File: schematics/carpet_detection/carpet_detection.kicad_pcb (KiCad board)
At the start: 2 copper layers, 7 parts, among them J1 Conn_01x03, U1 QRD1114, U2 TLC277

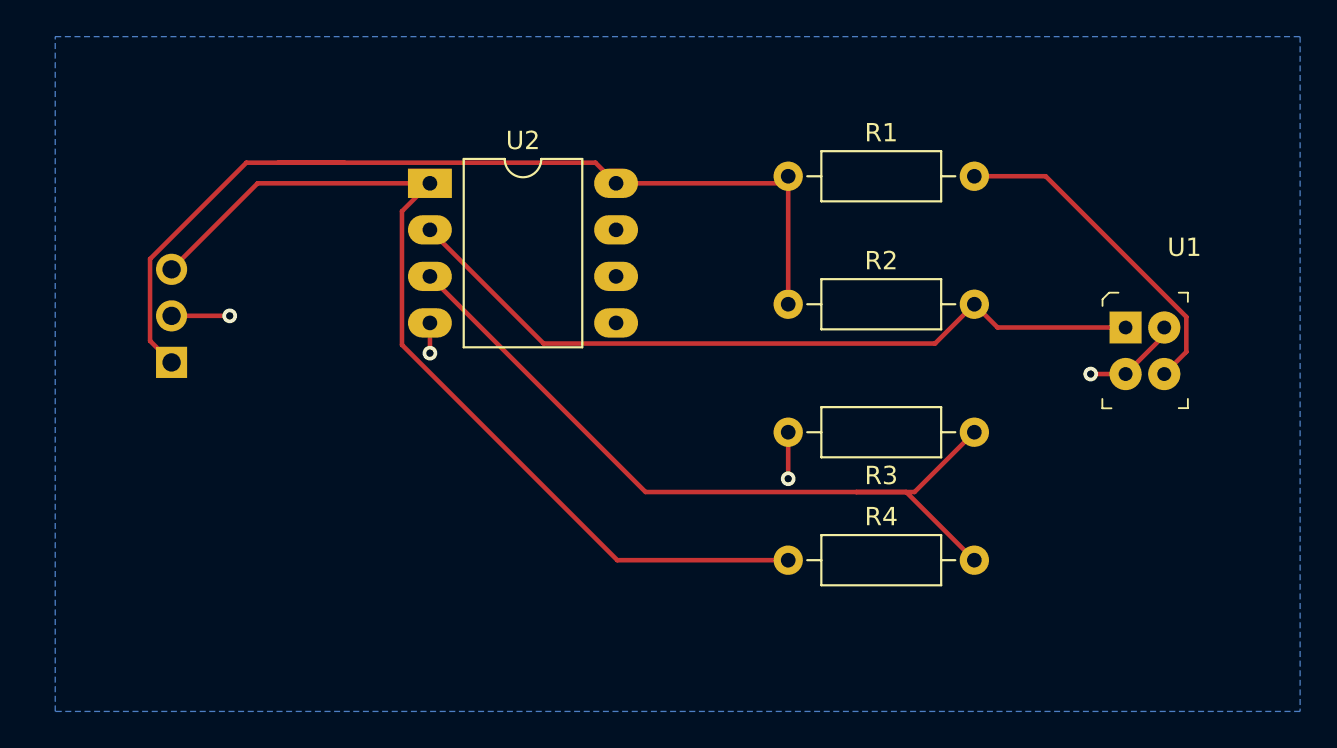
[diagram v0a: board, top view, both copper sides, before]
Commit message: Adds LEDS to the carpet detector
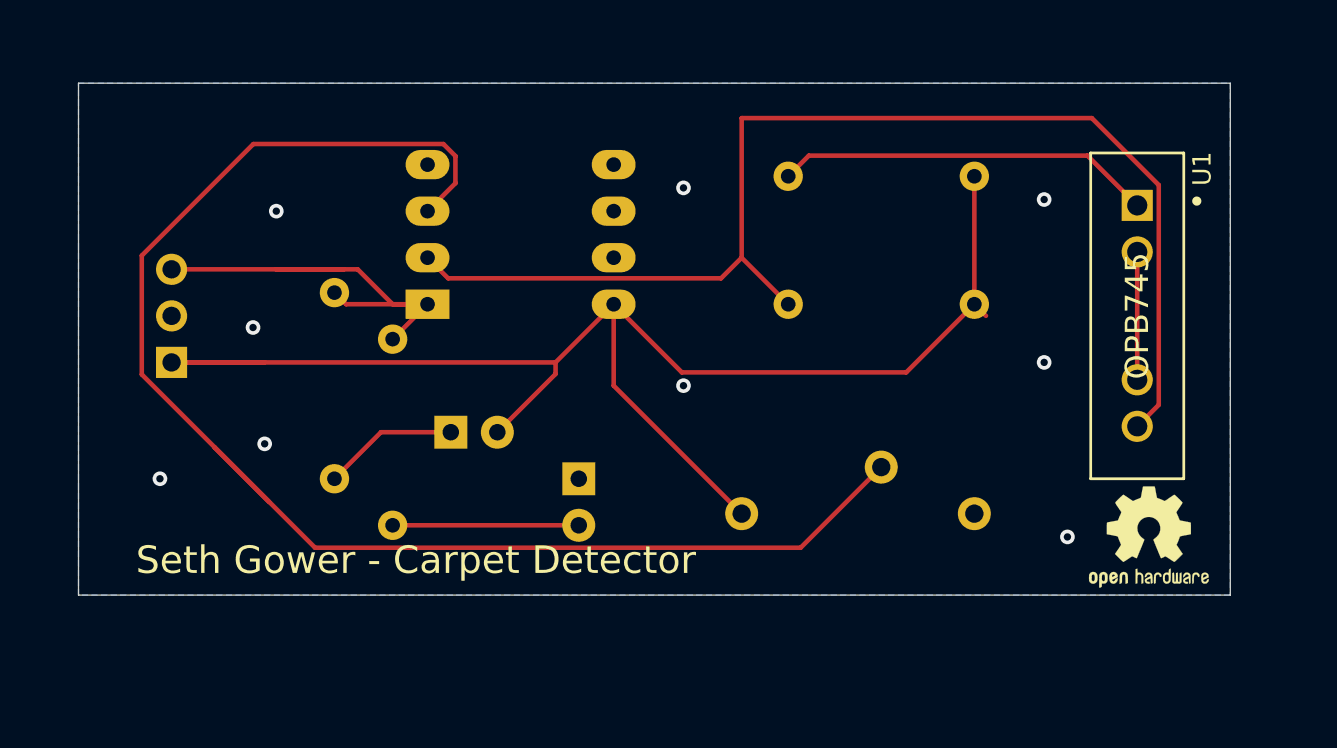
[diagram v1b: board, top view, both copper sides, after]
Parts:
- added D1: Red, LED_THT:LED_D4.0mm, B.Cu at (93.3, 101.6)
- added D2: Green, LED_THT:LED_D4.0mm, B.Cu at (100.3, 104.1)
- added REF**: OSHW-Logo2_7.3x6mm_SilkScreen, Symbol:OSHW-Logo2_7.3x6mm_SilkScreen, F.Cu at (131.4, 107.3)
- added REF**: OSHW-Logo2_7.3x6mm_SilkScreen, Symbol:OSHW-Logo2_7.3x6mm_SilkScreen, B.Cu at (131.4, 107.3)
- added RV1: R_POT_US, Potentiometer_THT:Potentiometer_Bourns_3005_Horizontal, B.Cu at (109.2, 106.0)
- R1, R2, U2: moved to B.Cu
- R3, R4: value R_US -> 1k; moved to B.Cu
- U1: value QRD1114 -> OPB745; footprint digikey-footprints:Reflective_Sensor_QRD1114 -> OPB745:TT_Electronics-OPB745-0
- moved R3 35.0 mm to (87.0, 104.1), turned to 90 degrees
- moved R4 24.7 mm to (90.2, 96.5), turned to 270 degrees
- moved R1 10.2 mm to (121.9, 87.6), turned to 180 degrees
- moved R2 10.2 mm to (121.9, 94.6), turned to 180 degrees
- moved U2 6.60 mm to (92.1, 94.6)
- moved U1 0.90 mm to (130.8, 95.2), turned to 270 degrees
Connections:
- net +5V renamed +3V3
- R2 pad 2: Net-(R2-Pad2) -> /Vin
- R3 pad 1: Net-(R3-Pad1) -> Net-(D1-Pad1)
- R3 pad 2: GND -> Vout
- R4 pad 2: Net-(R3-Pad1) -> Net-(D2-Pad2)
- U1 pad 1: Net-(R2-Pad2) -> Net-(R1-Pad2)
- U1 pad 3: Net-(R1-Pad2) -> GND
- U1 pad 4: GND -> /Vin
- U2 pad 2: Net-(R2-Pad2) -> /Vin
- U2 pad 3: Net-(R3-Pad1) -> /Vref
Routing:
- net /Vref: track 0.00 -> 80.4 mm
- net /Vin: track 0.00 -> 67.2 mm
- net Net-(R3-Pad1): track 43.9 -> 0.00 mm
- net Net-(R2-Pad2): track 42.0 -> 0.00 mm
- net +3V3: track 54.3 -> 80.5 mm
- net Vout: track 51.4 -> 26.5 mm
- net Net-(D2-Pad2): track 0.00 -> 10.2 mm
- net Net-(D1-Pad1): track 0.00 -> 7.40 mm
- net GND: track 12.7 -> 6.98 mm, vias 4 -> 9
- net Net-(R1-Pad2): track 18.4 -> 20.6 mm
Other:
- board outline added: 62.9 x 27.9 mm
- board text added: "Seth Gower - Carpet Detector"

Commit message: Removes Green LED, moves OPB745 to bottom, everything else to top
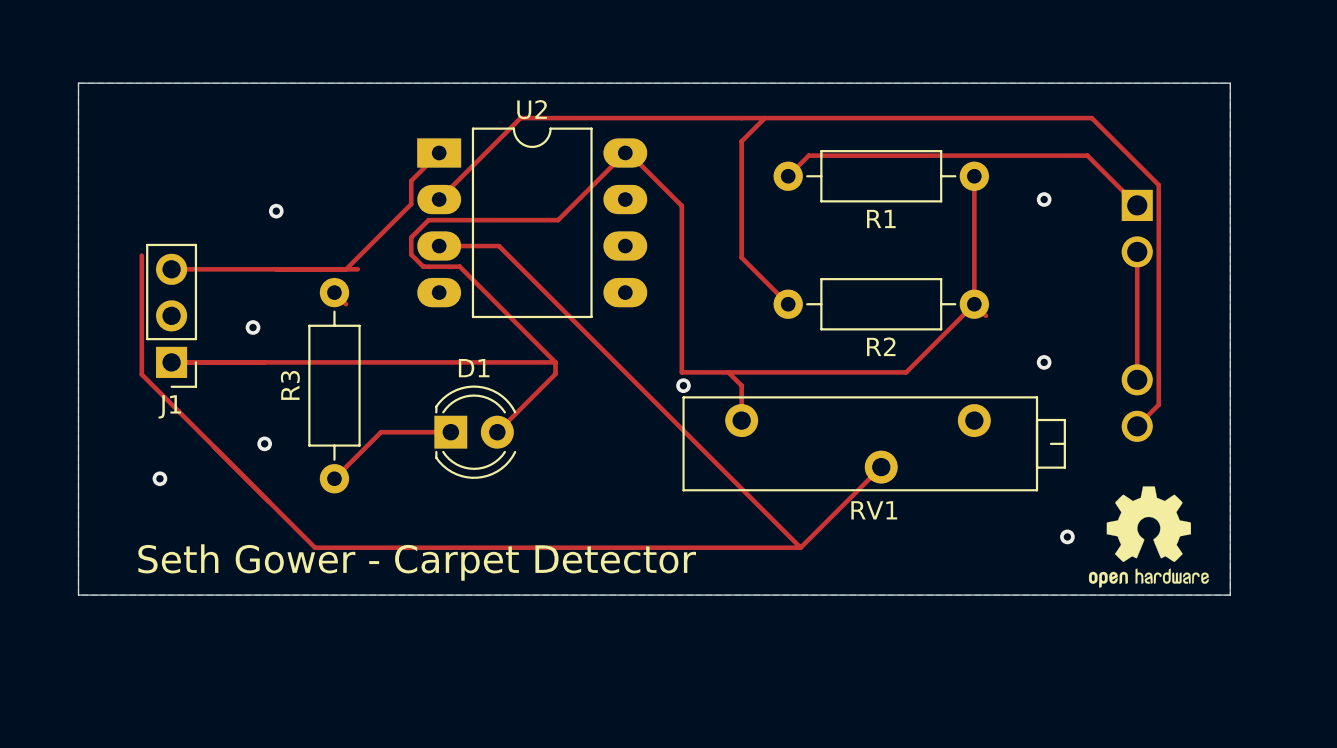
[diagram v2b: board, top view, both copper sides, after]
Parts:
- removed D2: Green, LED_THT:LED_D4.0mm
- removed R4: 1k, Resistor_THT:R_Axial_DIN0207_L6.3mm_D2.5mm_P10.16mm_Horizontal
- D1, J1, R1, R2, R3, U2: moved to F.Cu
- RV1: footprint Potentiometer_THT:Potentiometer_Bourns_3005_Horizontal -> Potentiometer_THT:Potentiometer_Bourns_3006P_Horizontal; moved to F.Cu
- U1: moved to B.Cu
- moved U2 8.28 mm to (92.7, 86.4)
- moved RV1 5.08 mm to (109.2, 101.0)
- turned J1 to 180 degrees
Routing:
- net +3V3: track 80.5 -> 97.6 mm
- net Net-(D2-Pad2): track 10.2 -> 0.00 mm
- net /Vref: track 80.4 -> 83.4 mm
- net Vout: track 26.5 -> 24.1 mm
- net /Vin: track 67.2 -> 68.0 mm
- net GND: vias 9 -> 8

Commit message: Final revision of the PCB. Ordered on OSH Park
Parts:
- D1: footprint LED_THT:LED_D4.0mm -> LED_THT:LED_D5.0mm
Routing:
- net /Vref: track 83.4 -> 29.1 mm
- net Vout: track 24.1 -> 28.2 mm
- net +3V3: track 97.6 -> 96.7 mm
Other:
- board text added: "3v3"
- board text added: "CMPE-460"
- board text added: "GND"
- board text added: "Seth Gower - Carpet Detector - 11/3/20"
- board text added: "Vout"
- board text removed: "Seth Gower - Carpet Detector"

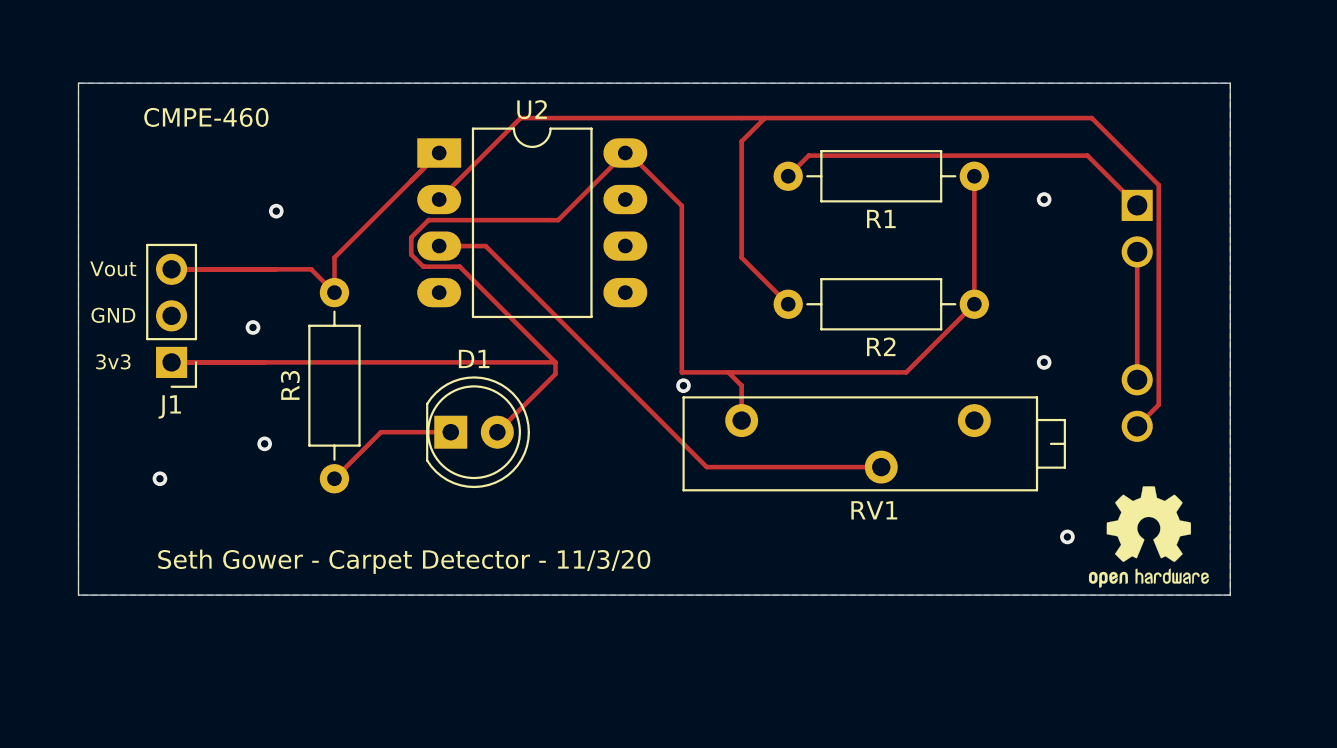
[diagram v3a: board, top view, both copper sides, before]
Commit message: Actually finishes the PCB.
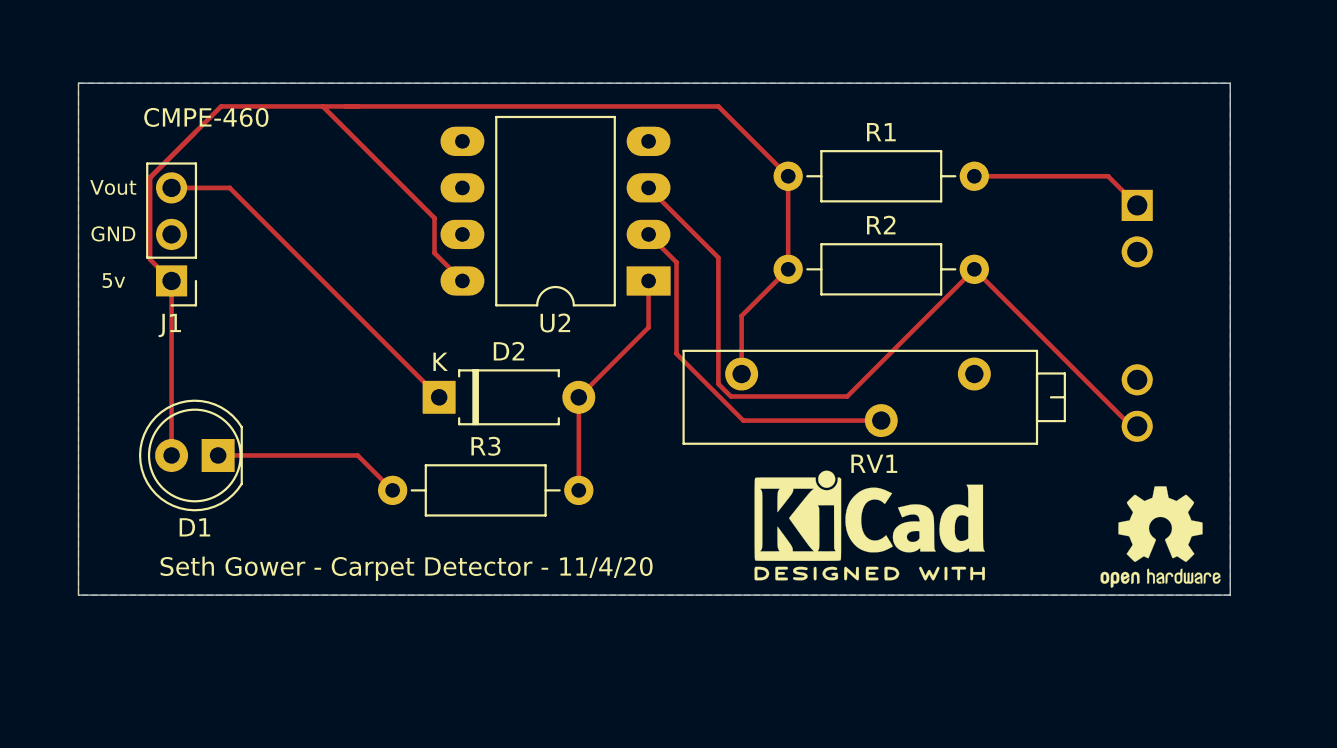
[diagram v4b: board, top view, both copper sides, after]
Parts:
- added D2: D, Diode_THT:D_A-405_P7.62mm_Horizontal, F.Cu at (92.7, 99.7)
- added REF**: KiCad-Logo2_5mm_SilkScreen, Symbol:KiCad-Logo2_5mm_SilkScreen, B.Cu at (92.7, 106.7)
- added REF**: KiCad-Logo2_5mm_SilkScreen, Symbol:KiCad-Logo2_5mm_SilkScreen, F.Cu at (116.2, 106.7)
- moved REF** 54.5 mm to (77.0, 107.3)
- moved U2 13.4 mm to (104.1, 93.3), turned to 180 degrees
- moved D1 12.8 mm to (80.6, 102.9), turned to 180 degrees
- moved R2 10.3 mm to (111.8, 92.7), turned to 0 degrees
- moved R1 10.2 mm to (111.8, 87.6), turned to 0 degrees
- moved J1 4.45 mm to (78.1, 93.3)
- moved R3 3.24 mm to (90.2, 104.8), turned to 0 degrees
- moved RV1 2.54 mm to (109.2, 98.4)
- moved REF** 0.64 mm to (132.1, 107.3)
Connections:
- net +3V3 renamed +5V
- R3 pad 2: Vout -> /Vo
- U2 pad 1: Vout -> /Vo
- U2 pad 2: /Vin -> /Vref
- U2 pad 3: /Vref -> /Vin
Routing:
- net /Vin: track 68.0 -> 41.8 mm
- net +5V: track 96.7 -> 82.9 mm
- net /Vo: track 0.00 -> 13.0 mm
- net Net-(R1-Pad2): track 20.6 -> 9.55 mm
- net /Vref: track 29.1 -> 19.8 mm
- net Vout: track 28.2 -> 19.3 mm
- net GND: track 6.98 -> 0.00 mm, vias 8 -> 0
- net Net-(D1-Pad1): track 7.40 -> 10.9 mm
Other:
- board text added: "5v"
- board text added: "Seth Gower - Carpet Detector - 11/4/20"
- board text removed: "3v3"
- board text removed: "Seth Gower - Carpet Detector - 11/3/20"
